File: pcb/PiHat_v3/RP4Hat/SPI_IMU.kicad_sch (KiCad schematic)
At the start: 3 parts, among them J7 Conn_01x08

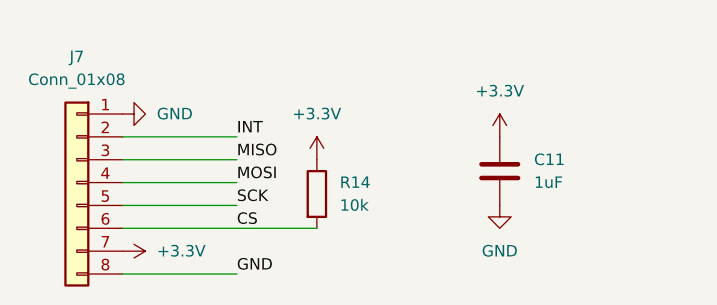
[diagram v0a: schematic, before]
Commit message: organize schematic further, no functional changes
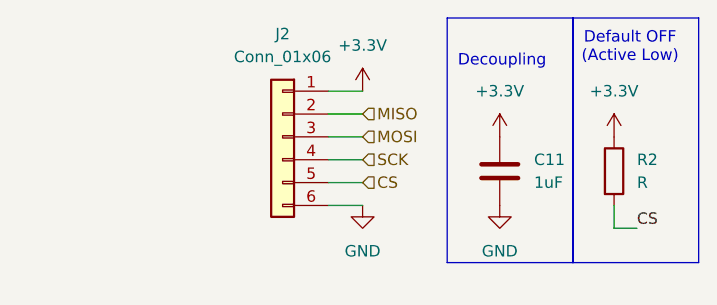
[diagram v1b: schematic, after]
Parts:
- removed J7: Conn_01x08, Connector_JST:JST_PH_S8B-PH-K_1x08_P2.00mm_Horizontal, symbol Connector_Generic:Conn_01x08
- removed R14: 10k, Resistor_SMD:R_0805_2012Metric_Pad1.20x1.40mm_HandSolder, symbol Device:R
- added J2: Conn_01x06, symbol Connector_Generic:Conn_01x06
- added R2: R, symbol Device:R
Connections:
- net +3.3V: now also J2.1 (Pin_1), R2.1
- net CS: now also J2.5 (Pin_5), R2.2
- net GND: now also J2.6 (Pin_6)
- net MISO: now also J2.2 (Pin_2)
- net MOSI: now also J2.3 (Pin_3)
- net SCK: now also J2.4 (Pin_4)
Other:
- note added: "Decoupling"
- note added: "Default OFF (Active Low)"

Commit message: big potato shi
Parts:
- J2: footprint (none) -> Connector_JST:JST_PH_S6B-PH-K_1x06_P2.00mm_Horizontal
- R2: value R -> 10k; footprint (none) -> Resistor_SMD:R_0805_2012Metric_Pad1.20x1.40mm_HandSolder
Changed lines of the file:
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@@
 			)
 		)
-		(property "Value" "R"
+		(property "Value" "10k"
 			(at 166.37 100.3299 0)
 			(show_name no)
@@
 			)
 		)
-		(property "Footprint" ""
+		(property "Footprint" "Resistor_SMD:R_0805_2012Metric_Pad1.20x1.40mm_HandSolder"
 			(at 162.052 99.06 90)
 			(hide yes)
@@
 			)
 		)
-		(property "Footprint" ""
+		(property "Footprint" "Connector_JST:JST_PH_S6B-PH-K_1x06_P2.00mm_Horizontal"
 			(at 127 95.25 0)
 			(hide yes)
